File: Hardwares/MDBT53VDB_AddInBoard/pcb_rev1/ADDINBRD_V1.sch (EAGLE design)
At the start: 22 parts, among them CN1 51296-0894, CN2 IF_6PIN, CN3 IF_3PIN, CN4 IF_4PIN, CN5 IF_2PIN_H, Q1 BSS84AKQBZ, U1 RV-3028-C7

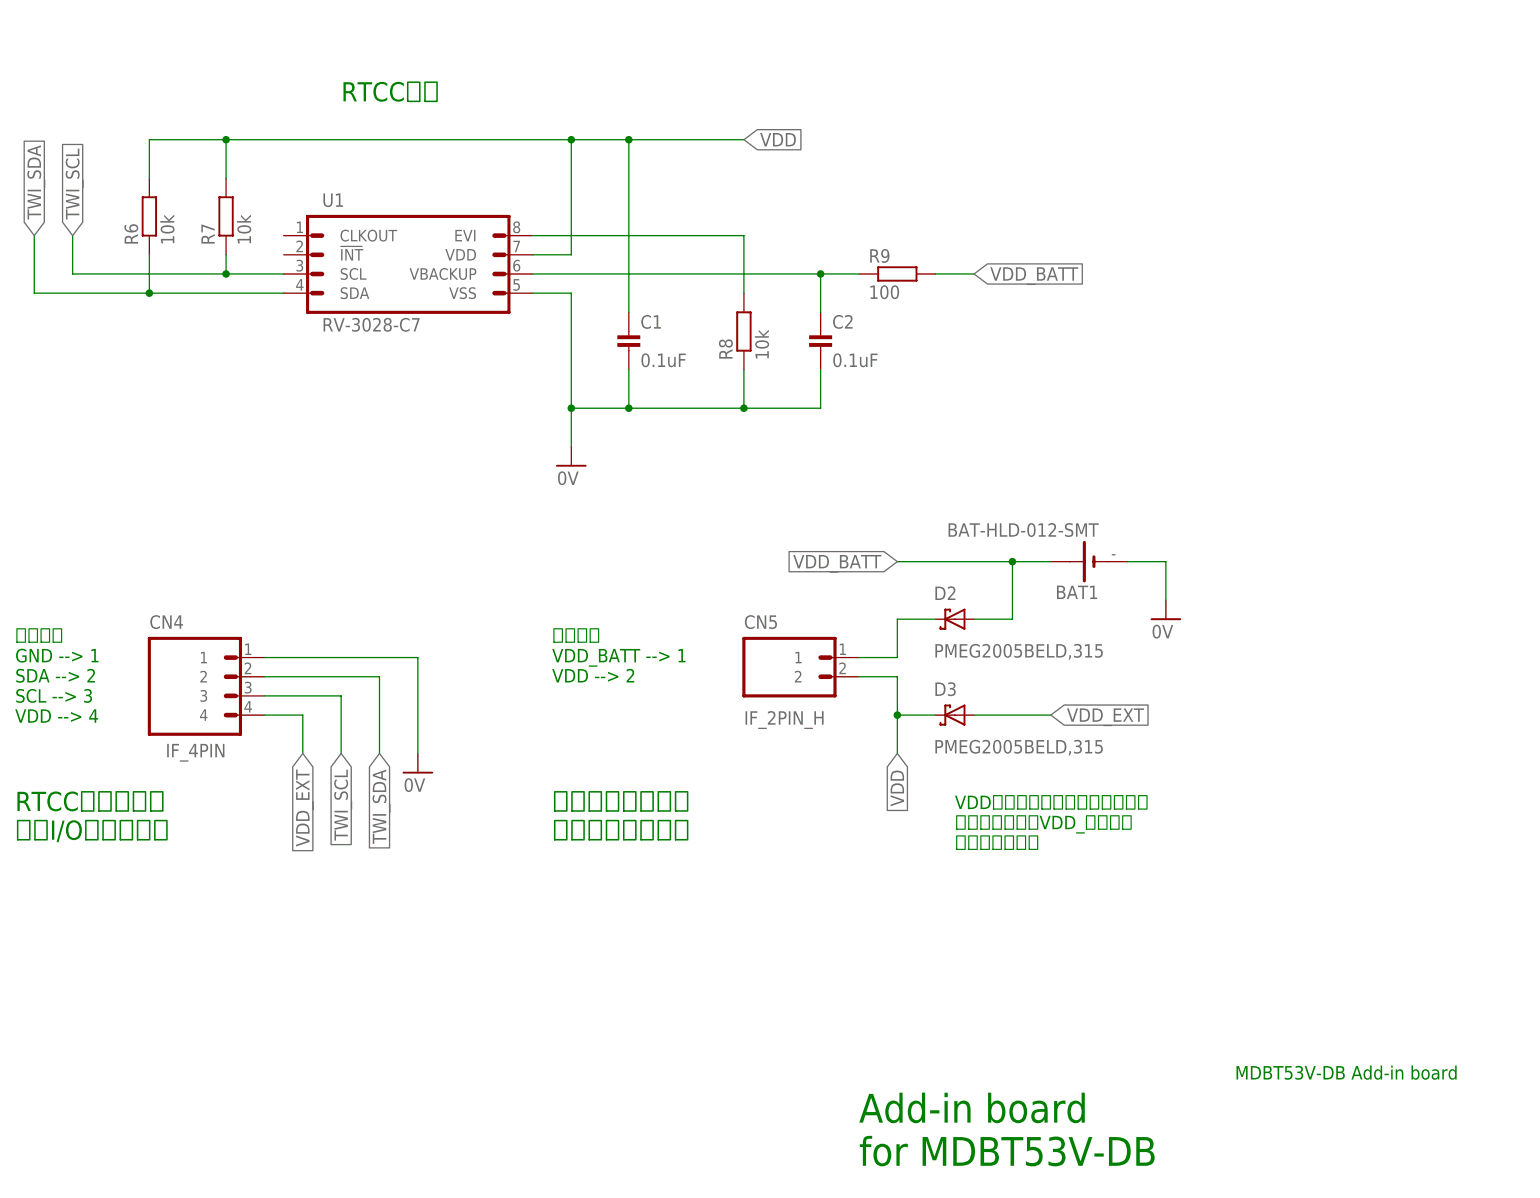
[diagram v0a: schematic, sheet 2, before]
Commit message: 回路図を修正
・リセット回路の追加
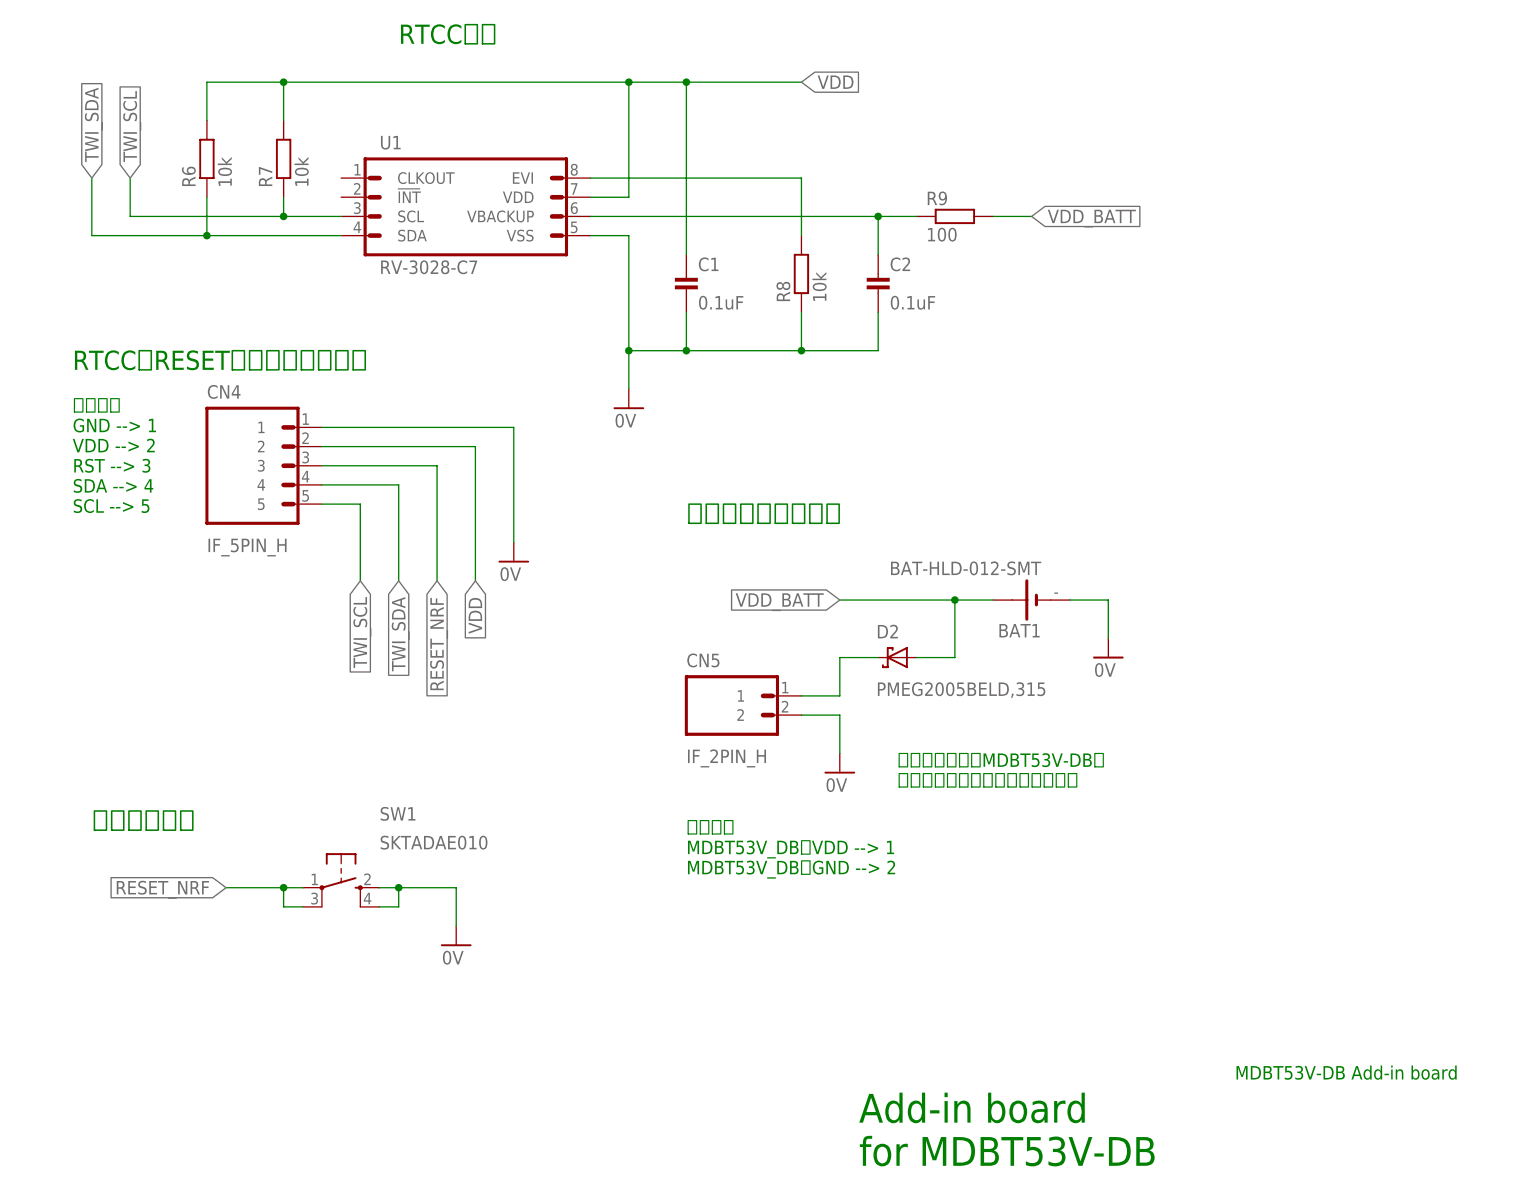
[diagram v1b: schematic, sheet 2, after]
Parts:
- removed D3: PMEG2005BELD,315, Parts:PMEG2005BELD,315
- added SW1: SKTADAE010, Parts:SKTADAE010
- CN4: value IF_4PIN -> IF_5PIN_H; device Connectors:IF_4PIN -> Connectors:IF_5PIN_H
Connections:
- removed net VDD_EXT: CN4.4, D3.A
- new net RESET_NRF: CN4.3, SW1.P, SW1.P1
- net 0V: now also CN5.2, SW1.S, SW1.S1
- net TWI_SCL: now also CN4.5; no longer CN4.3
- net TWI_SDA: now also CN4.4; no longer CN4.2
- net VDD: now also CN4.2; no longer CN5.2, D3.C
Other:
- note added: "RTCC／RESET制御配線用ポート"
- note added: "ピン対応 GND --> 1 VDD --> 2 RST --> 3 SDA --> 4 SCL --> 5"
- note added: "ピン対応 MDBT53V_DBのVDD --> 1 MDBT53V_DBのGND --> 2"
- note added: "ボタン電池からMDBT53V-DBに 電源を供給するためのピンです。"
- note added: "ボタン電池電源回路"
- note added: "リセット回路"
- note removed: "RTCC回路接続用 汎用I/O接続ポート"
- note removed: "VDDが外部電源に未接続の場合、 ボタン電池からVDD_に電源が 供給されます。"
- note removed: "ピン対応 GND --> 1 SDA --> 2 SCL --> 3 VDD --> 4"
- note removed: "ピン対応 VDD_BATT --> 1 VDD --> 2"
- note removed: "ボタン電池からの 電源供給切り替え"
- moved on the sheet: BAT1, C1, C2, CN5, D2, R6, R7, R8, R9, U1

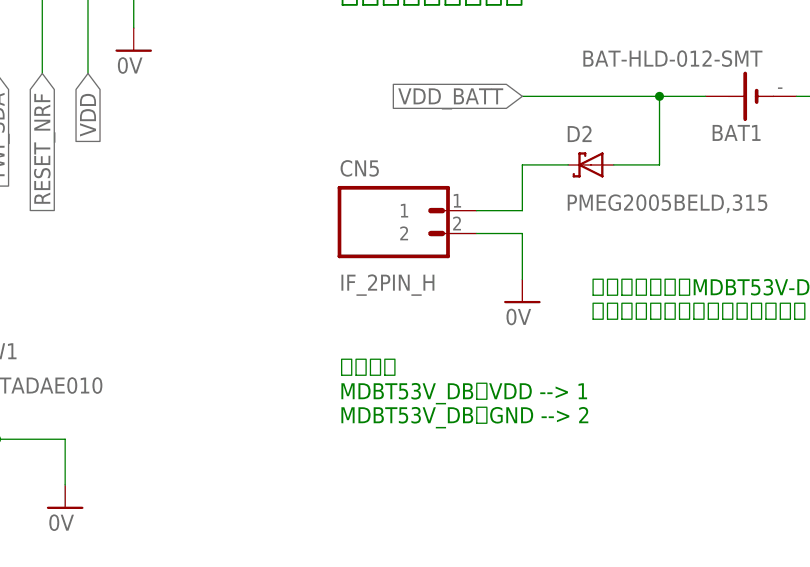
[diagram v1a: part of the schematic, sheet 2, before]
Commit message: 回路図を修正
・パッケージ名を変更
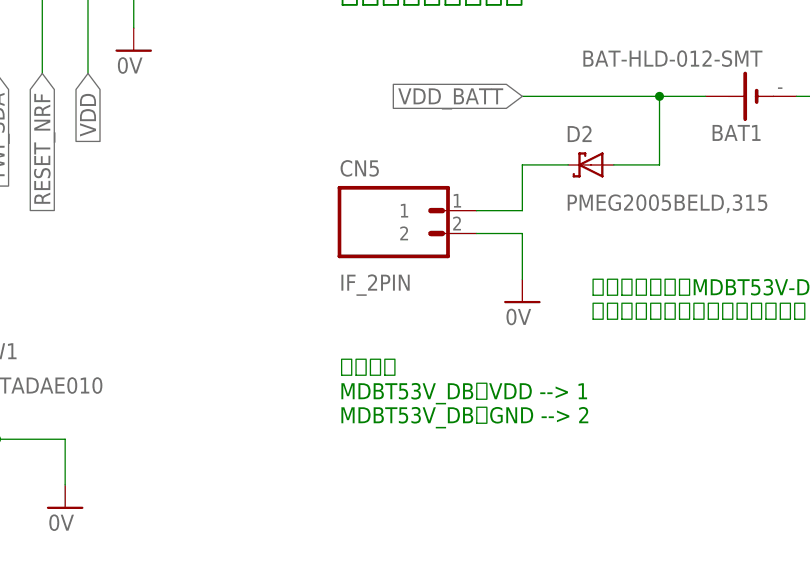
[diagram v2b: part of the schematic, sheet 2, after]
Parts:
- CN5: value IF_2PIN_H -> IF_2PIN; device Connectors:IF_2PIN_H -> Connectors:IF_2PIN
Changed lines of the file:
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@@
 <part name="C2" library="Parts" deviceset="CAP" device="_0402N" value="0.1uF"/>
 <part name="R9" library="Parts" deviceset="RESISTOR" device="_0402N" value="100"/>
-<part name="CN5" library="Connectors" deviceset="IF_2PIN" device="_H"/>
+<part name="CN5" library="Connectors" deviceset="IF_2PIN" device=""/>
 <part name="BAT1" library="Connectors" deviceset="BAT-HLD-012-SMT" device=""/>
 <part name="GND5" library="Supply" deviceset="0V" device=""/>

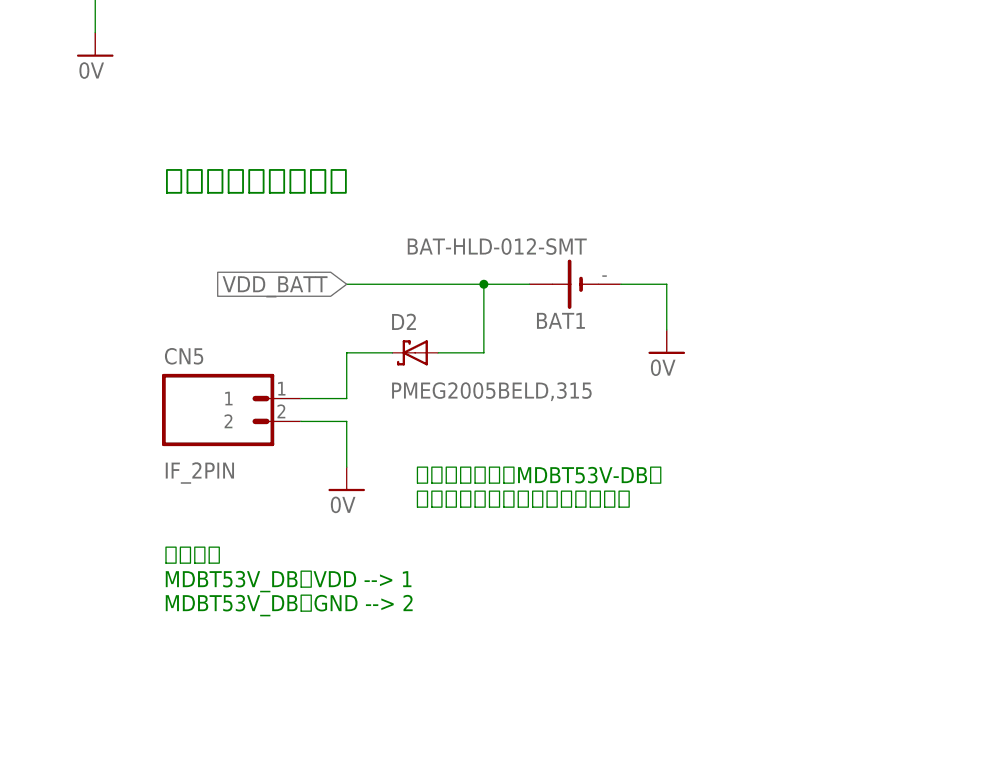
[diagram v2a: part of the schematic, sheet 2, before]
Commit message: 回路図を修正
・ピン割り当てが逆転していたので修正
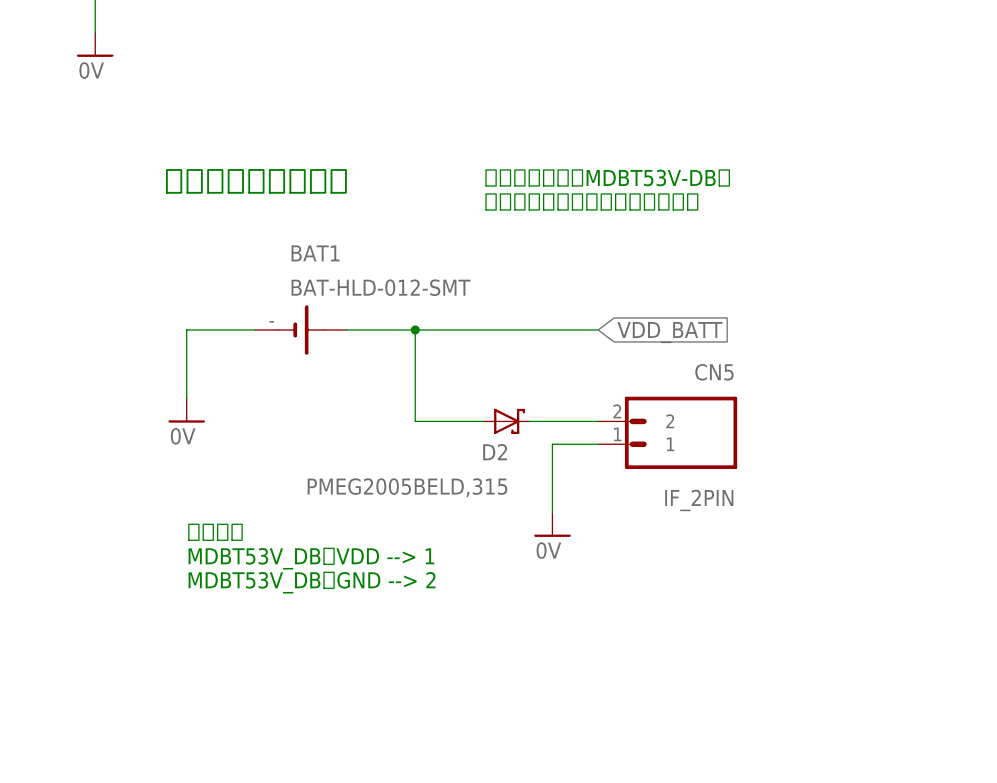
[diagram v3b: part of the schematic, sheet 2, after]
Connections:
- net 0V: now also CN5.1; no longer CN5.2
- net N$2: now also CN5.2; no longer CN5.1
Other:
- moved on the sheet: BAT1, CN5, D2
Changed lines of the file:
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@@
 for MDBT53V-DB</text>
 <text x="144.78" y="96.52" size="2.54" layer="91" align="top-left">ボタン電池電源回路</text>
-<text x="144.78" y="54.61" size="1.778" layer="91" align="top-left">ピン対応
+<text x="147.32" y="57.15" size="1.778" layer="91" align="top-left">ピン対応
 MDBT53V_DBのVDD --&gt; 1
 MDBT53V_DBのGND --&gt; 2</text>
-<text x="172.72" y="63.5" size="1.778" layer="91" align="top-left">ボタン電池からMDBT53V-DBに
+<text x="180.34" y="96.52" size="1.778" layer="91" align="top-left">ボタン電池からMDBT53V-DBに
 電源を供給するためのピンです。</text>
 <text x="66.04" y="55.88" size="2.54" layer="91" align="top-left">リセット回路</text>
@@
 <instance part="C2" gate="G$1" x="170.18" y="129.54"/>
 <instance part="R9" gate="G$1" x="175.26" y="134.62"/>
-<instance part="CN5" gate="G$1" x="160.02" y="68.58" smashed="yes" rot="R180">
-<attribute name="VALUE" x="144.78" y="62.23" size="1.778" layer="96"/>
-<attribute name="NAME" x="144.78" y="74.93" size="1.778" layer="95"/>
-</instance>
-<instance part="BAT1" gate="G$1" x="190.5" y="83.82" rot="R180"/>
-<instance part="GND5" gate="1" x="200.66" y="76.2"/>
-<instance part="D2" gate="G$1" x="172.72" y="76.2" smashed="yes" rot="R180">
-<attribute name="NAME" x="169.926" y="78.74" size="1.778" layer="95"/>
-<attribute name="VALUE" x="169.926" y="71.12" size="1.778" layer="96"/>
+<instance part="CN5" gate="G$1" x="193.04" y="68.58" smashed="yes">
+<attribute name="VALUE" x="208.28" y="60.96" size="1.778" layer="96" rot="R180"/>
+<attribute name="NAME" x="208.28" y="74.93" size="1.778" layer="95" rot="R180"/>
+</instance>
+<instance part="BAT1" gate="G$1" x="160.02" y="78.74" smashed="yes">
+<attribute name="NAME" x="158.75" y="86.36" size="1.778" layer="95"/>
+<attribute name="VALUE" x="158.75" y="82.55" size="1.778" layer="96"/>
+</instance>
+<instance part="GND5" gate="1" x="147.32" y="68.58"/>
+<instance part="D2" gate="G$1" x="182.88" y="68.58" smashed="yes">
+<attribute name="NAME" x="183.134" y="66.04" size="1.778" layer="95" rot="R180"/>
+<attribute name="VALUE" x="183.134" y="62.23" size="1.778" layer="96" rot="R180"/>
 </instance>
 <instance part="CN4" gate="G$1" x="96.52" y="96.52" smashed="yes" rot="R180">
@@
 <attribute name="NAME" x="81.28" y="110.49" size="1.778" layer="95"/>
 </instance>
-<instance part="GND3" gate="1" x="165.1" y="60.96"/>
+<instance part="GND3" gate="1" x="187.96" y="55.88"/>
 <instance part="SW1" gate="G$1" x="99.06" y="45.72" smashed="yes" rot="R270">
 <attribute name="NAME" x="104.14" y="54.61" size="1.778" layer="95"/>
@@
 </segment>
 <segment>
-<pinref part="BAT1" gate="G$1" pin="-"/>
-<pinref part="GND5" gate="1" pin="0V"/>
-<wire x1="195.58" y1="83.82" x2="200.66" y2="83.82" width="0.1524" layer="91"/>
-<wire x1="200.66" y1="83.82" x2="200.66" y2="78.74" width="0.1524" layer="91"/>
-</segment>
-<segment>
 <pinref part="CN4" gate="G$1" pin="1"/>
 <pinref part="GND4" gate="1" pin="0V"/>
 <wire x1="96.52" y1="106.68" x2="121.92" y2="106.68" width="0.1524" layer="91"/>
 <wire x1="121.92" y1="106.68" x2="121.92" y2="91.44" width="0.1524" layer="91"/>
-</segment>
-<segment>
-<pinref part="CN5" gate="G$1" pin="2"/>
-<pinref part="GND3" gate="1" pin="0V"/>
-<wire x1="160.02" y1="68.58" x2="165.1" y2="68.58" width="0.1524" layer="91"/>
-<wire x1="165.1" y1="68.58" x2="165.1" y2="63.5" width="0.1524" layer="91"/>
 </segment>
 <segment>
@@
 <wire x1="114.3" y1="45.72" x2="114.3" y2="40.64" width="0.1524" layer="91"/>
 <junction x="106.68" y="45.72"/>
+</segment>
+<segment>
+<pinref part="CN5" gate="G$1" pin="1"/>
+<pinref part="GND3" gate="1" pin="0V"/>
+<wire x1="193.04" y1="66.04" x2="187.96" y2="66.04" width="0.1524" layer="91"/>
+<wire x1="187.96" y1="66.04" x2="187.96" y2="58.42" width="0.1524" layer="91"/>
+</segment>
+<segment>
+<pinref part="BAT1" gate="G$1" pin="-"/>
+<pinref part="GND5" gate="1" pin="0V"/>
+<wire x1="154.94" y1="78.74" x2="147.32" y2="78.74" width="0.1524" layer="91"/>
+<wire x1="147.32" y1="78.74" x2="147.32" y2="71.12" width="0.1524" layer="91"/>
 </segment>
 </net>
@@
 <segment>
 <pinref part="BAT1" gate="G$1" pin="+"/>
-<wire x1="185.42" y1="83.82" x2="180.34" y2="83.82" width="0.1524" layer="91"/>
-<label x="165.1" y="83.82" size="1.778" layer="95" rot="R180" xref="yes"/>
-<junction x="180.34" y="83.82"/>
-<wire x1="180.34" y1="83.82" x2="165.1" y2="83.82" width="0.1524" layer="91"/>
+<wire x1="165.1" y1="78.74" x2="172.72" y2="78.74" width="0.1524" layer="91"/>
+<wire x1="172.72" y1="78.74" x2="193.04" y2="78.74" width="0.1524" layer="91"/>
+<wire x1="172.72" y1="78.74" x2="172.72" y2="68.58" width="0.1524" layer="91"/>
 <pinref part="D2" gate="G$1" pin="A"/>
-<wire x1="175.26" y1="76.2" x2="180.34" y2="76.2" width="0.1524" layer="91"/>
-<wire x1="180.34" y1="76.2" x2="180.34" y2="83.82" width="0.1524" layer="91"/>
-</segment>
-</net>
-<net name="N$2" class="0">
-<segment>
-<pinref part="CN5" gate="G$1" pin="1"/>
-<wire x1="160.02" y1="71.12" x2="165.1" y2="71.12" width="0.1524" layer="91"/>
-<wire x1="165.1" y1="71.12" x2="165.1" y2="76.2" width="0.1524" layer="91"/>
-<pinref part="D2" gate="G$1" pin="C"/>
-<wire x1="165.1" y1="76.2" x2="170.18" y2="76.2" width="0.1524" layer="91"/>
+<wire x1="172.72" y1="68.58" x2="180.34" y2="68.58" width="0.1524" layer="91"/>
+<label x="193.04" y="78.74" size="1.778" layer="95" xref="yes"/>
+<junction x="172.72" y="78.74"/>
 </segment>
 </net>
@@
 </segment>
 </net>
+<net name="N$2" class="0">
+<segment>
+<pinref part="CN5" gate="G$1" pin="2"/>
+<pinref part="D2" gate="G$1" pin="C"/>
+<wire x1="193.04" y1="68.58" x2="185.42" y2="68.58" width="0.1524" layer="91"/>
+</segment>
+</net>
